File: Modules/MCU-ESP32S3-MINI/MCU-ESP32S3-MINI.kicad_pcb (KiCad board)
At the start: 4 copper layers, 27 x 24 mm, 11 parts, among them SW1 BOOT, SW2 RESET, U1 ESP32-S3-MINI-1-N8

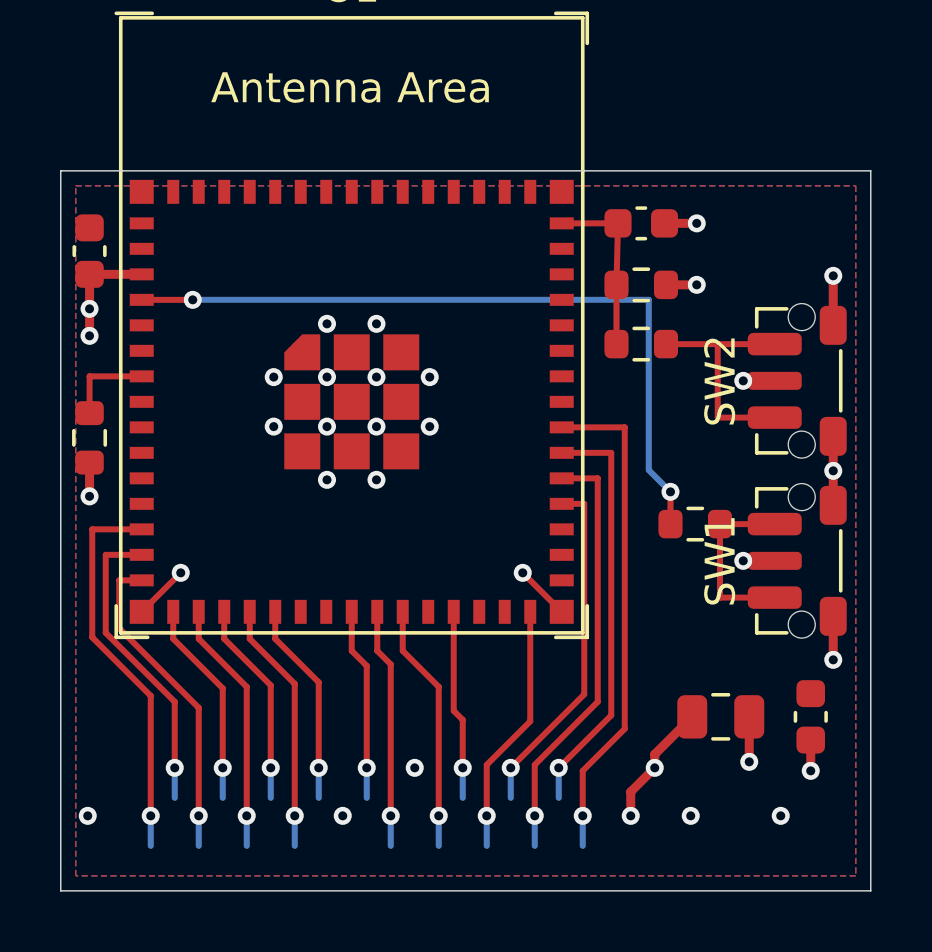
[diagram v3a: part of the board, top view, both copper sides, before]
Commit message: Apply the review fixes to five boards and set solid power pads
Plans were proven on scratch copies, then applied with KiCad's own pcbnew
Python API, so KiCad writes every file. Each board: DRC 0 errors, 0
unconnected, 0 parity, and the canary fires.

Ethernet and PoE module (R1-1, R1-2, R1-3):
- The fanout rule no longer matches zones.
- Chip-side copper keeps 1.0 mm from the line-side jack pads (was 0.26 mm):
  MDI_RDP, MDI_RDN, RCT and LED_LINK_K rerouted. A 1.0 mm rule enforces it.
  The VC1P lane passes J2.8 at 0.42 mm inside the jack pad field, and only
  that pair is excepted.
- GND vias: Ethernet 8 to 42, PoE 11 to 55. No starved thermal remains.

Buck (R2-2, R2-5): three GND vias at U8.1, C100.2 and C101.2. TP3 sits
against R61.1, with a courtyard rule scoped to that pair.
USBC (R2-4): U2 moves 3 mm toward J1, with two GND vias at U2.2.
MCU (R1-9): C2 sits 1.71 mm from U1 pin 3 (was 23.5 mm), with a courtyard
rule scoped to C2 and U1.
Solid zone connections (R2-3) on U8, L30, C100 to C104, C108 to C111 and J1.

Co-Authored-By: Claude Opus 5.5 (1M context) <noreply@anthropic.com>
Claude-Session: https://claude.ai/code/session_01ErAAfkmF4h3T5yfrw21utF
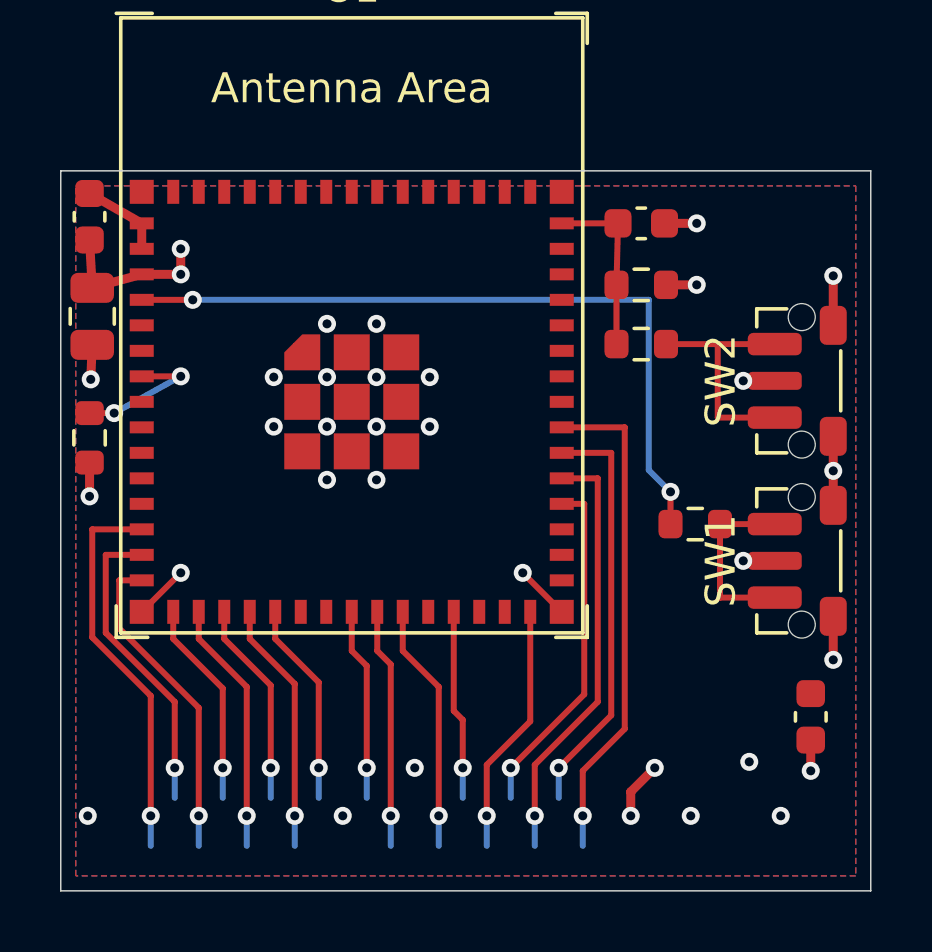
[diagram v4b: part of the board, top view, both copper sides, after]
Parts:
- moved C2 24.8 mm to (101.0, 104.8), turned to -90 degrees
- moved C3 1.14 mm to (101.0, 101.5)
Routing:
- net GND: track 14.9 -> 17.4 mm, vias 27 -> 28
- net Net-(U1-IO3): track 2.97 -> 4.66 mm, vias 0 -> 2
- net +3V3: track 9.99 -> 9.44 mm
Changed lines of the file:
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@@
 	(footprint "Capacitor_SMD:C_0603_1608Metric"
 		(layer "F.Cu")
-		(at 100.96 102.675 90)
+		(at 100.96 101.53 90)
 		(descr "Capacitor SMD 0603 (1608 Metric), square (rectangular) end terminal, IPC-7351 nominal, (Body size source: IPC-SM-782 page 76, https://www.pcb-3d.com/wordpress/wp-content/uploads/ipc-sm-782a_amendment_1_and_2.pdf)")
 		(tags "capacitor")
@@
 	(footprint "Capacitor_SMD:C_0805_2012Metric"
 		(layer "F.Cu")
-		(at 122 118.2)
+		(at 101.05 104.85 -90)
 		(descr "Capacitor SMD 0805 (2012 Metric), square (rectangular) end terminal, IPC-7351 nominal, (Body size source: IPC-SM-782 page 76, https://www.pcb-3d.com/wordpress/wp-content/uploads/ipc-sm-782a_amendment_1_and_2.pdf, https://docs.google.com/spreadsheets/d/1BsfQQcO9C6DZCsRaXUlFlo91Tg2WpOkGARC1WS5S8t0/edit?usp=sharing)")
 		(tags "capacitor")
 		(property "Reference" "C2"
-			(at 0 -1.68 0)
+			(at 0 -1.68 270)
 			(layer "F.Fab")
 			(effects
@@
 		)
 		(property "Value" "22uF 25V X5R"
-			(at 0 1.68 0)
+			(at 0 1.68 270)
 			(layer "F.Fab")
 			(effects
@@
 		)
 		(property "Datasheet" ""
-			(at 0 0 0)
+			(at 0 0 270)
 			(layer "F.Fab")
 			(hide yes)
@@
 		)
 		(property "Description" ""
-			(at 0 0 0)
+			(at 0 0 270)
 			(layer "F.Fab")
 			(hide yes)
@@
 		)
 		(property "KiLib_Generator" "SMD_2terminal_chip_molded"
-			(at 0 0 0)
+			(at 0 0 270)
 			(layer "F.SilkS")
 			(hide yes)
@@
 		)
 		(property "MPN" "CL21A226MAQNNNE"
-			(at 0 0 0)
+			(at 0 0 270)
 			(unlocked yes)
 			(layer "F.Fab")
@@
 		)
 		(property "Manufacturer" "Samsung Electro-Mechanics"
-			(at 0 0 0)
+			(at 0 0 270)
 			(unlocked yes)
 			(layer "F.Fab")
@@
 		(duplicate_pad_numbers_are_jumpers no)
 		(fp_line
+			(start -0.261252 0.735)
+			(end 0.261252 0.735)
+			(stroke
+				(width 0.12)
+				(type solid)
+			)
+			(layer "F.SilkS")
+		)
+		(fp_line
 			(start -0.261252 -0.735)
 			(end 0.261252 -0.735)
-			(stroke
-				(width 0.12)
-				(type solid)
-			)
-			(layer "F.SilkS")
-		)
-		(fp_line
-			(start -0.261252 0.735)
-			(end 0.261252 0.735)
 			(stroke
 				(width 0.12)
@@
 		)
 		(fp_text user "${REFERENCE}"
-			(at 0 0 0)
+			(at 0 0 270)
 			(layer "F.Fab")
 			(effects
@@
 		)
 		(pad "1" smd roundrect
-			(at -0.95 0)
+			(at -0.95 0 270)
 			(size 1 1.45)
 			(layers "F.Cu" "F.Mask" "F.Paste")
@@
 		)
 		(pad "2" smd roundrect
-			(at 0.95 0)
+			(at 0.95 0 270)
 			(size 1 1.45)
 			(layers "F.Cu" "F.Mask" "F.Paste")
@@
 	)
 	(segment
-		(start 119.8 119.45)
-		(end 119.8 119.9)
+		(start 102.7 103.45)
+		(end 104 103.45)
 		(width 0.3)
 		(layer "F.Cu")
@@
 	)
 	(segment
-		(start 100.96 104.6)
-		(end 100.96 105.5)
-		(width 0.3)
-		(layer "F.Cu")
-		(net "+3V3")
-	)
-	(segment
-		(start 102.7 103.45)
-		(end 100.96 103.45)
-		(width 0.3)
-		(layer "F.Cu")
-		(net "+3V3")
-	)
-	(segment
-		(start 100.96 103.45)
-		(end 100.96 104.6)
+		(start 100.96 102.305)
+		(end 101.05 103.9)
 		(width 0.3)
 		(layer "F.Cu")
@@
 	)
 	(segment
-		(start 121.05 118.2)
-		(end 119.8 119.45)
+		(start 102.7 103.45)
+		(end 101.05 103.9)
 		(width 0.3)
 		(layer "F.Cu")
@@
 		(net "+3V3")
 	)
-	(via
-		(at 100.96 105.5)
-		(size 0.6)
-		(drill 0.3)
-		(layers "F.Cu" "B.Cu")
+	(segment
+		(start 104 103.45)
+		(end 104 102.6)
+		(width 0.3)
+		(layer "F.Cu")
 		(net "+3V3")
 	)
@@
 	)
 	(via
-		(at 100.96 104.6)
+		(at 104 103.45)
+		(size 0.6)
+		(drill 0.3)
+		(layers "F.Cu" "B.Cu")
+		(net "+3V3")
+	)
+	(via
+		(at 104 102.6)
 		(size 0.6)
 		(drill 0.3)
@@
 	)
 	(segment
+		(start 101.05 105.8)
+		(end 101 106.95)
+		(width 0.3)
+		(layer "F.Cu")
+		(net "GND")
+	)
+	(segment
 		(start 125.75 108.85)
 		(end 125.75 110)
@@
 	)
 	(segment
+		(start 102.7 101.75)
+		(end 102.7 102.6)
+		(width 0.3)
+		(layer "F.Cu")
+		(net "GND")
+	)
+	(segment
 		(start 125.75 105.15)
 		(end 125.75 103.5)
@@
 	)
 	(segment
+		(start 100.96 100.755)
+		(end 102.7 101.75)
+		(width 0.3)
+		(layer "F.Cu")
+		(net "GND")
+	)
+	(segment
 		(start 123.8 113)
 		(end 122.75 113)
@@
 	)
 	(segment
-		(start 122.95 118.2)
-		(end 122.95 119.7)
-		(width 0.3)
-		(layer "F.Cu")
-		(net "GND")
-	)
-	(segment
 		(start 100.96 109.725)
 		(end 100.96 110.85)
@@
 	)
 	(via
+		(at 101 106.95)
+		(size 0.6)
+		(drill 0.3)
+		(layers "F.Cu" "B.Cu")
+		(net "GND")
+	)
+	(via
 		(at 104 113.4)
 		(size 0.6)
@@
 	)
 	(segment
-		(start 100.96 106.85)
+		(start 102.7 106.85)
+		(end 104 106.85)
+		(width 0.2)
+		(layer "F.Cu")
+		(net "Net-(U1-IO3)")
+	)
+	(segment
+		(start 101.78 108.075)
 		(end 100.96 108.075)
 		(width 0.2)
@@
 		(net "Net-(U1-IO3)")
 	)
-	(segment
-		(start 102.7 106.85)
-		(end 100.96 106.85)
+	(via
+		(at 104 106.85)
+		(size 0.6)
+		(drill 0.3)
+		(layers "F.Cu" "B.Cu")
+		(net "Net-(U1-IO3)")
+	)
+	(via
+		(at 101.78 108.075)
+		(size 0.6)
+		(drill 0.3)
+		(layers "F.Cu" "B.Cu")
+		(net "Net-(U1-IO3)")
+	)
+	(segment
+		(start 104 106.85)
+		(end 101.78 108.075)
 		(width 0.2)
-		(layer "F.Cu")
+		(layer "B.Cu")
 		(net "Net-(U1-IO3)")
 	)

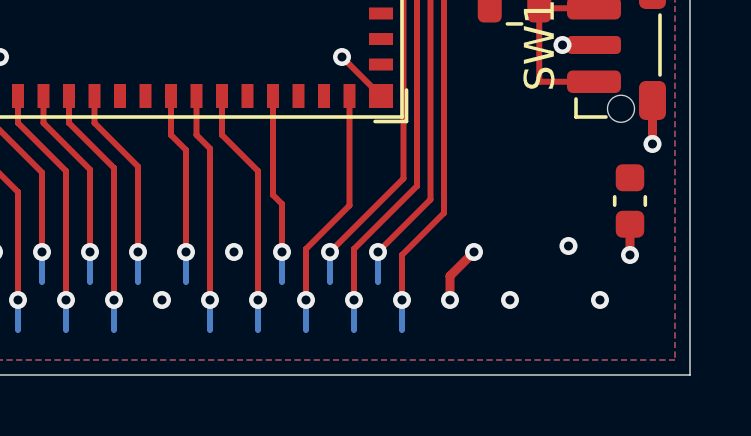
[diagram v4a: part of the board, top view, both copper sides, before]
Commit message: Add the MCU +3V3 breakout stub and bring Modules.md up to date
The +3V3 breakout via on the MCU board had no stub (review R1-10). It now
has a 1.0 mm B.Cu stub like the other row vias. DRC 0 errors, and
track_dangling rises from 17 to 18, one per stub. Fragment rebuilt.

Modules.md: global library rows only, the full module set, and the
Host-Setup page in the list of what every module carries.

Co-Authored-By: Claude Opus 5.5 (1M context) <noreply@anthropic.com>
Claude-Session: https://claude.ai/code/session_01ErAAfkmF4h3T5yfrw21utF
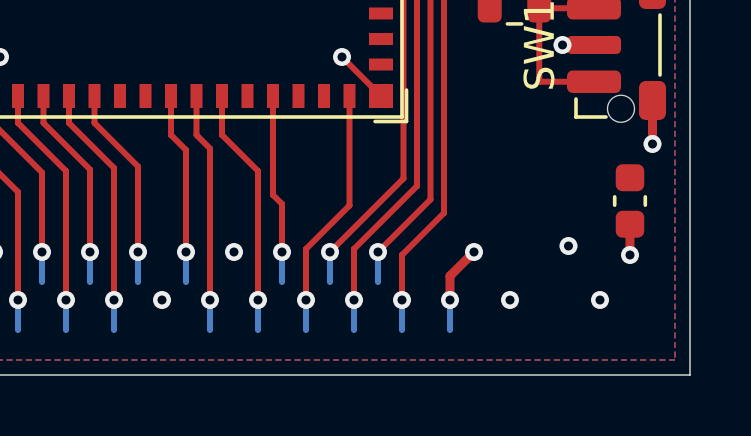
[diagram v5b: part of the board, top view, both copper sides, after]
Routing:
- net +3V3: track 9.44 -> 10.4 mm
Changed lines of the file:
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@@
+	)
+	(segment
+		(start 119 121.5)
+		(end 119 122.5)
+		(width 0.2)
+		(layer "B.Cu")
+		(net "+3V3")
 	)
 	(segment
